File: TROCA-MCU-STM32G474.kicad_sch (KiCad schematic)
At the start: 15 parts, among them SW1 HX-3X6X2.5-X SMD TACT SWITCH, SW2 HX-3X6X2.5-X SMD TACT SWITCH, U3 STM32G474VETx, X1 X32258MOB4SI

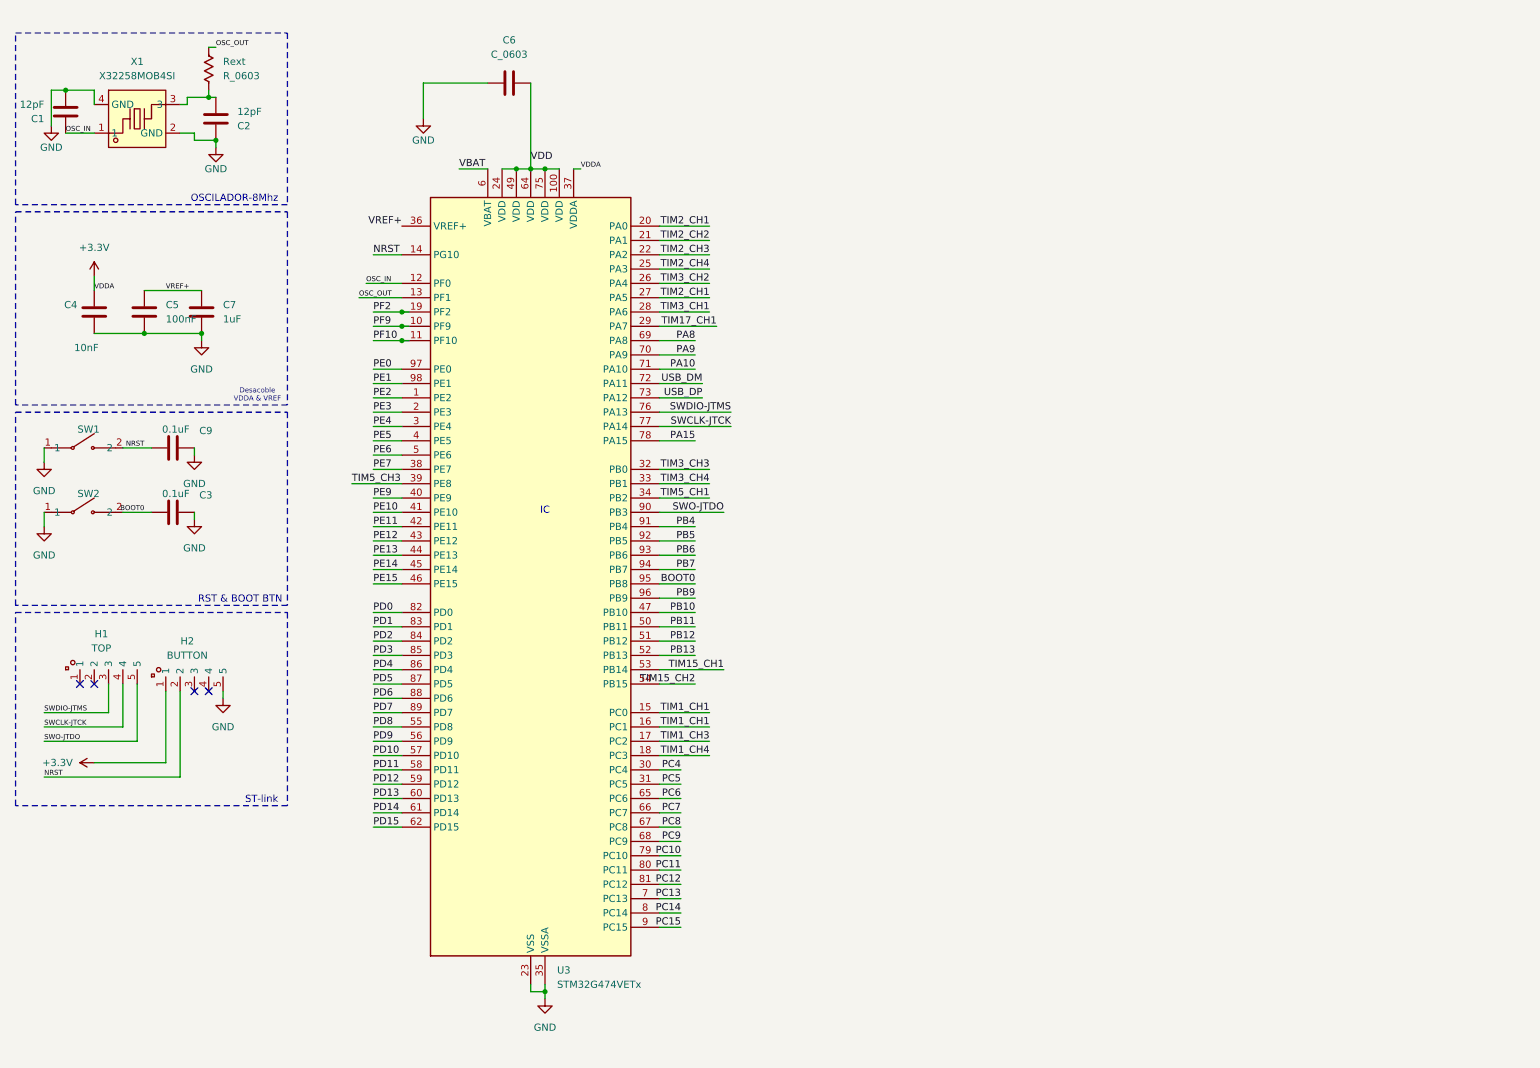
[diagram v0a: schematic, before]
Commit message: Datasheet stm32G474 añadido & declaracion de pines
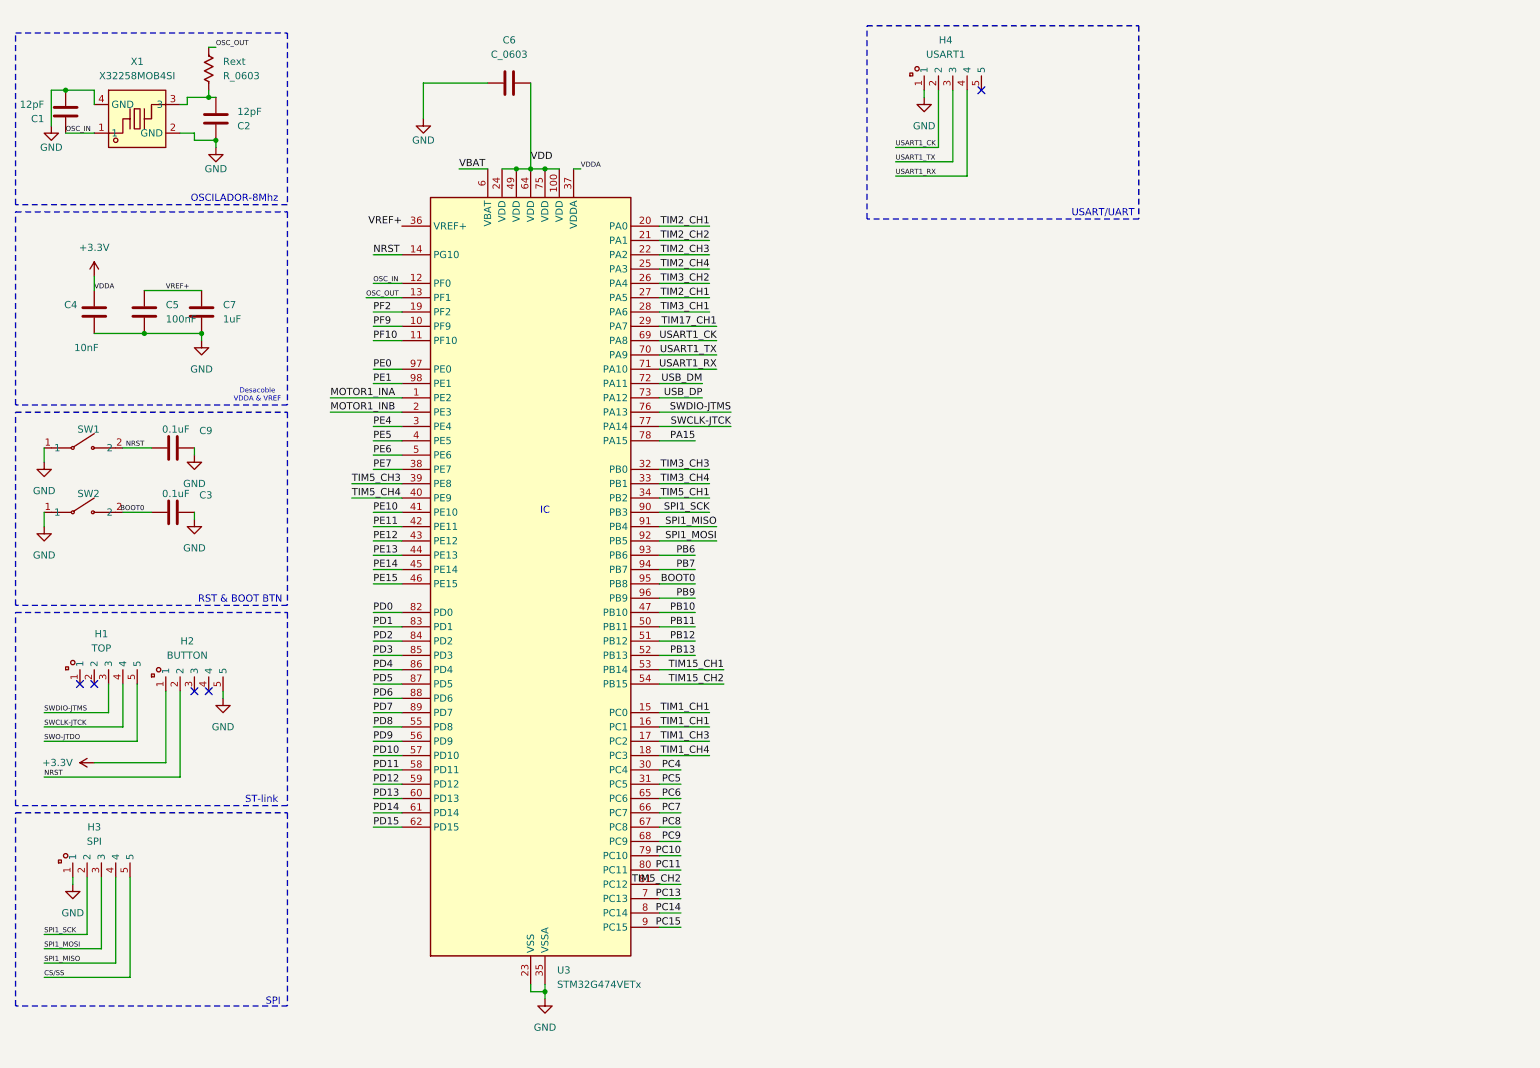
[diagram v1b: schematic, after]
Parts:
- added H3: SPI, EasyEDA:HDR-TH_5P-P2.00-V-M, symbol EasyEDA:HXPZ2.0-1X5PZZ
- added H4: USART1, EasyEDA:HDR-TH_5P-P2.00-V-M, symbol EasyEDA:HXPZ2.0-1X5PZZ
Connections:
- net GND: now also H3.1, H4.1
- net SWO-JTDO: no longer U3.90 (PB3)
- net PA10 renamed USART1_RX
- net USART1_RX: now also H4.4
- net PA8 renamed USART1_CK
- net USART1_CK: now also H4.2
- net PA9 renamed USART1_TX
- net USART1_TX: now also H4.3
- net PB4 renamed SPI1_MISO
- net SPI1_MISO: now also H3.4
- net PB5 renamed SPI1_MOSI
- net SPI1_MOSI: now also H3.3
- net PC12 renamed TIM5_CH2
- net PE2 renamed MOTOR1_INA
- net PE3 renamed MOTOR1_INB
- net PE9 renamed TIM5_CH4
- new net CS/SS: H3.5
- new net SPI1_SCK: H3.2, U3.90 (PB3)
- no-connect marks 4 -> 5
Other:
- note added: "SPI"
- note added: "USART/UART"

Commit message: Delcaracion de INA & INB drivers de motores
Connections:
- net PD0 renamed MOTOR6_INA
- net PD1 renamed MOTOR6_INB
- net PD2 renamed MOTOR7_INA
- net PD3 renamed MOTOR7_INB
- net PD4 renamed MOTOR8_INA
- net PD5 renamed MOTOR8_INB
- net PE10 renamed MOTOR4_INA
- net PE11 renamed MOTOR4_INB
- net PE12 renamed MOTOR5_INA
- net PE13 renamed MOTOR5_INB
- net PE4 renamed MOTOR2_INA
- net PE5 renamed MOTOR2_INB
- net PE6 renamed MOTOR3_INA
- net PE7 renamed MOTOR3_INB
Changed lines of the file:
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@@
 	(wire
 		(pts
-			(xy 80.01 104.14) (xy 85.09 104.14)
+			(xy 72.39 104.14) (xy 85.09 104.14)
 		)
 		(stroke
@@
 	(wire
 		(pts
-			(xy 80.01 121.92) (xy 85.09 121.92)
+			(xy 72.39 121.92) (xy 85.09 121.92)
 		)
 		(stroke
@@
 	(wire
 		(pts
-			(xy 80.01 86.36) (xy 85.09 86.36)
+			(xy 72.39 86.36) (xy 85.09 86.36)
 		)
 		(stroke
@@
 	(wire
 		(pts
-			(xy 80.01 88.9) (xy 85.09 88.9)
+			(xy 72.39 88.9) (xy 85.09 88.9)
 		)
 		(stroke
@@
 	(wire
 		(pts
-			(xy 80.01 127) (xy 85.09 127)
+			(xy 72.39 127) (xy 85.09 127)
 		)
 		(stroke
@@
 	(wire
 		(pts
-			(xy 134.62 167.64) (xy 130.81 167.64)
+			(xy 139.7 167.64) (xy 130.81 167.64)
 		)
 		(stroke
@@
 	(wire
 		(pts
-			(xy 80.01 101.6) (xy 85.09 101.6)
+			(xy 72.39 101.6) (xy 85.09 101.6)
 		)
 		(stroke
@@
 	(wire
 		(pts
-			(xy 80.01 132.08) (xy 85.09 132.08)
-		)
-		(stroke
-			(width 0)
-			(type default)
-		)
-	)
-	(wire
-		(pts
-			(xy 80.01 129.54) (xy 85.09 129.54)
+			(xy 72.39 132.08) (xy 85.09 132.08)
+		)
+		(stroke
+			(width 0)
+			(type default)
+		)
+	)
+	(wire
+		(pts
+			(xy 72.39 129.54) (xy 85.09 129.54)
 		)
 		(stroke
@@
 	(wire
 		(pts
-			(xy 80.01 119.38) (xy 85.09 119.38)
+			(xy 72.39 119.38) (xy 85.09 119.38)
 		)
 		(stroke
@@
 	(wire
 		(pts
-			(xy 80.01 93.98) (xy 85.09 93.98)
+			(xy 72.39 93.98) (xy 85.09 93.98)
 		)
 		(stroke
@@
 	(wire
 		(pts
-			(xy 80.01 124.46) (xy 85.09 124.46)
+			(xy 72.39 124.46) (xy 85.09 124.46)
 		)
 		(stroke
@@
 	(wire
 		(pts
-			(xy 80.01 91.44) (xy 85.09 91.44)
+			(xy 72.39 91.44) (xy 85.09 91.44)
 		)
 		(stroke
@@
 		)
 	)
-	(label "PE6"
-		(at 80.01 91.44 0)
+	(label "MOTOR3_INA"
+		(at 72.39 91.44 0)
 		(effects
 			(font
@@
 		)
 	)
-	(label "PD5"
-		(at 80.01 132.08 0)
+	(label "MOTOR8_INB"
+		(at 72.39 132.08 0)
 		(effects
 			(font
@@
 		)
 	)
-	(label "PD0"
-		(at 80.01 119.38 0)
+	(label "MOTOR6_INA"
+		(at 72.39 119.38 0)
 		(effects
 			(font
@@
 		)
 	)
-	(label "PE11"
-		(at 80.01 104.14 0)
+	(label "MOTOR4_INB"
+		(at 72.39 104.14 0)
 		(effects
 			(font
@@
 		)
 	)
-	(label "PE4"
-		(at 80.01 86.36 0)
+	(label "MOTOR2_INA"
+		(at 72.39 86.36 0)
 		(effects
 			(font
@@
 		)
 	)
-	(label "PD4"
-		(at 80.01 129.54 0)
+	(label "MOTOR8_INA"
+		(at 72.39 129.54 0)
 		(effects
 			(font
@@
 		)
 	)
-	(label "PE7"
-		(at 80.01 93.98 0)
+	(label "MOTOR3_INB"
+		(at 72.39 93.98 0)
 		(effects
 			(font
@@
 	)
 	(label "TIM5_CH2"
-		(at 134.62 167.64 180)
+		(at 139.7 167.64 180)
 		(effects
 			(font
@@
 		)
 	)
-	(label "PE10"
-		(at 80.01 101.6 0)
+	(label "MOTOR4_INA"
+		(at 72.39 101.6 0)
 		(effects
 			(font
@@
 		)
 	)
-	(label "PE12"
+	(label "MOTOR5_INA"
 		(at 80.01 106.68 0)
 		(effects
@@
 		)
 	)
-	(label "PD1"
-		(at 80.01 121.92 0)
+	(label "MOTOR6_INB"
+		(at 72.39 121.92 0)
 		(effects
 			(font
@@
 		)
 	)
-	(label "PD3"
-		(at 80.01 127 0)
-		(effects
-			(font
-				(size 1.27 1.27)
-			)
-			(justify left bottom)
-		)
-	)
-	(label "PE5"
-		(at 80.01 88.9 0)
+	(label "MOTOR7_INB"
+		(at 72.39 127 0)
+		(effects
+			(font
+				(size 1.27 1.27)
+			)
+			(justify left bottom)
+		)
+	)
+	(label "MOTOR2_INB"
+		(at 72.39 88.9 0)
 		(effects
 			(font
@@
 		)
 	)
-	(label "PD2"
-		(at 80.01 124.46 0)
+	(label "MOTOR7_INA"
+		(at 72.39 124.46 0)
 		(effects
 			(font
@@
 		)
 	)
-	(label "PE13"
+	(label "MOTOR5_INB"
 		(at 80.01 109.22 0)
 		(effects

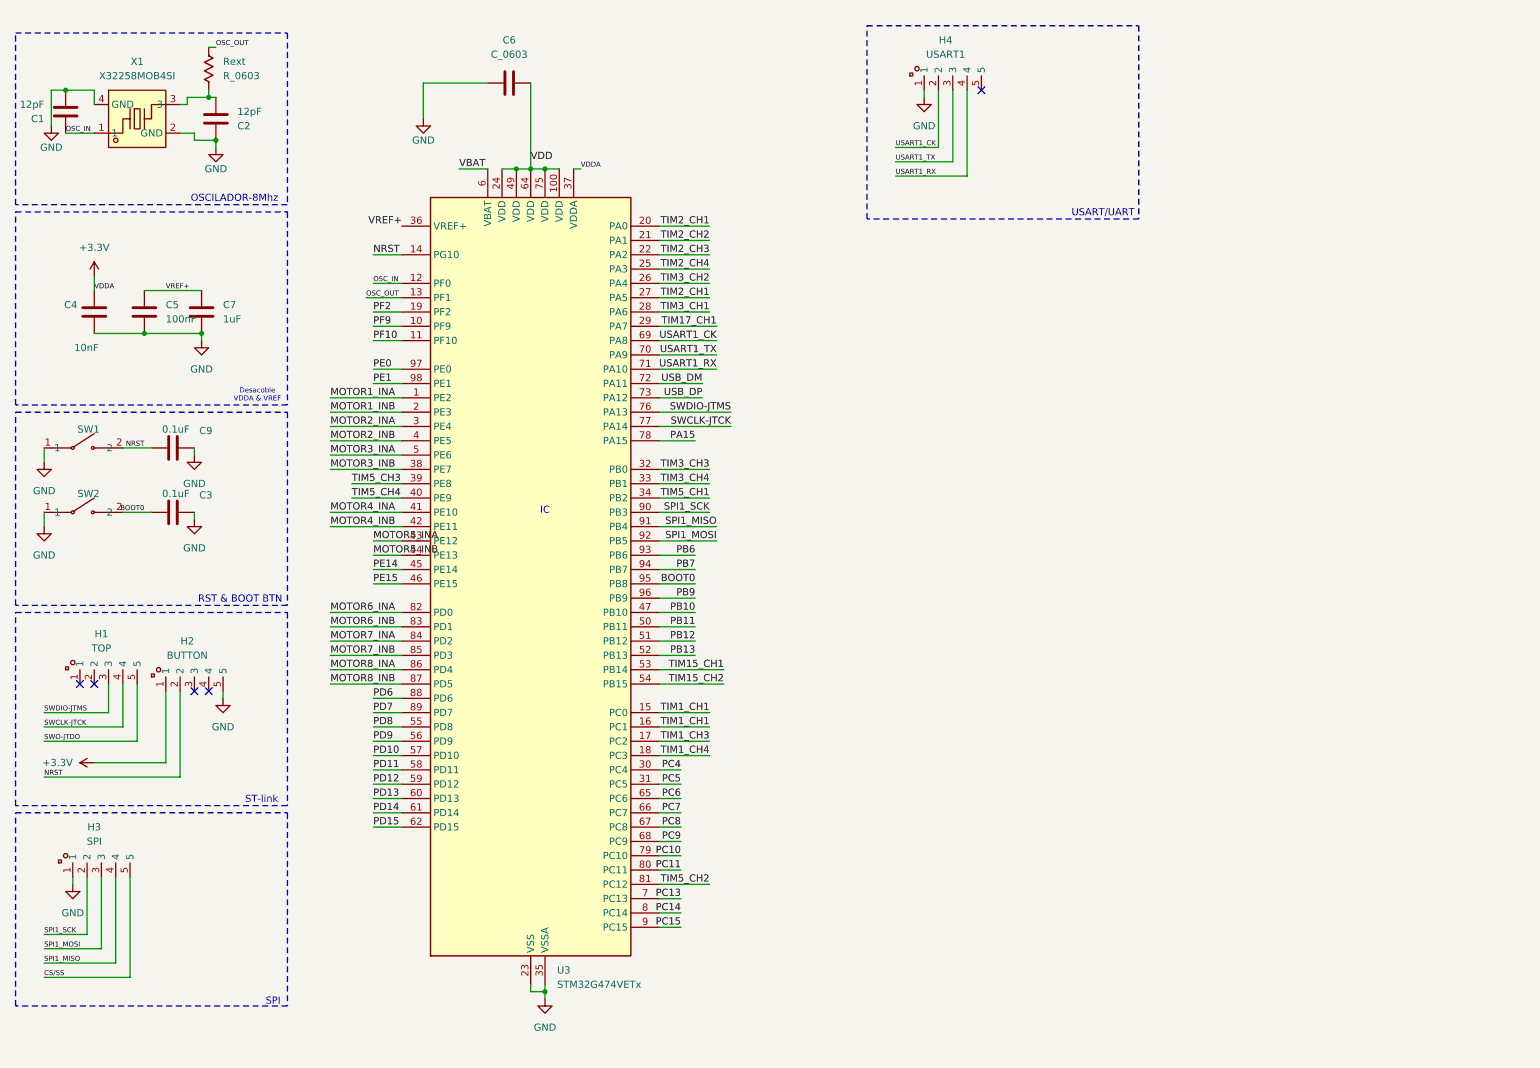
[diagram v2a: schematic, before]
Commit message: Ajustes de asignacion de pines
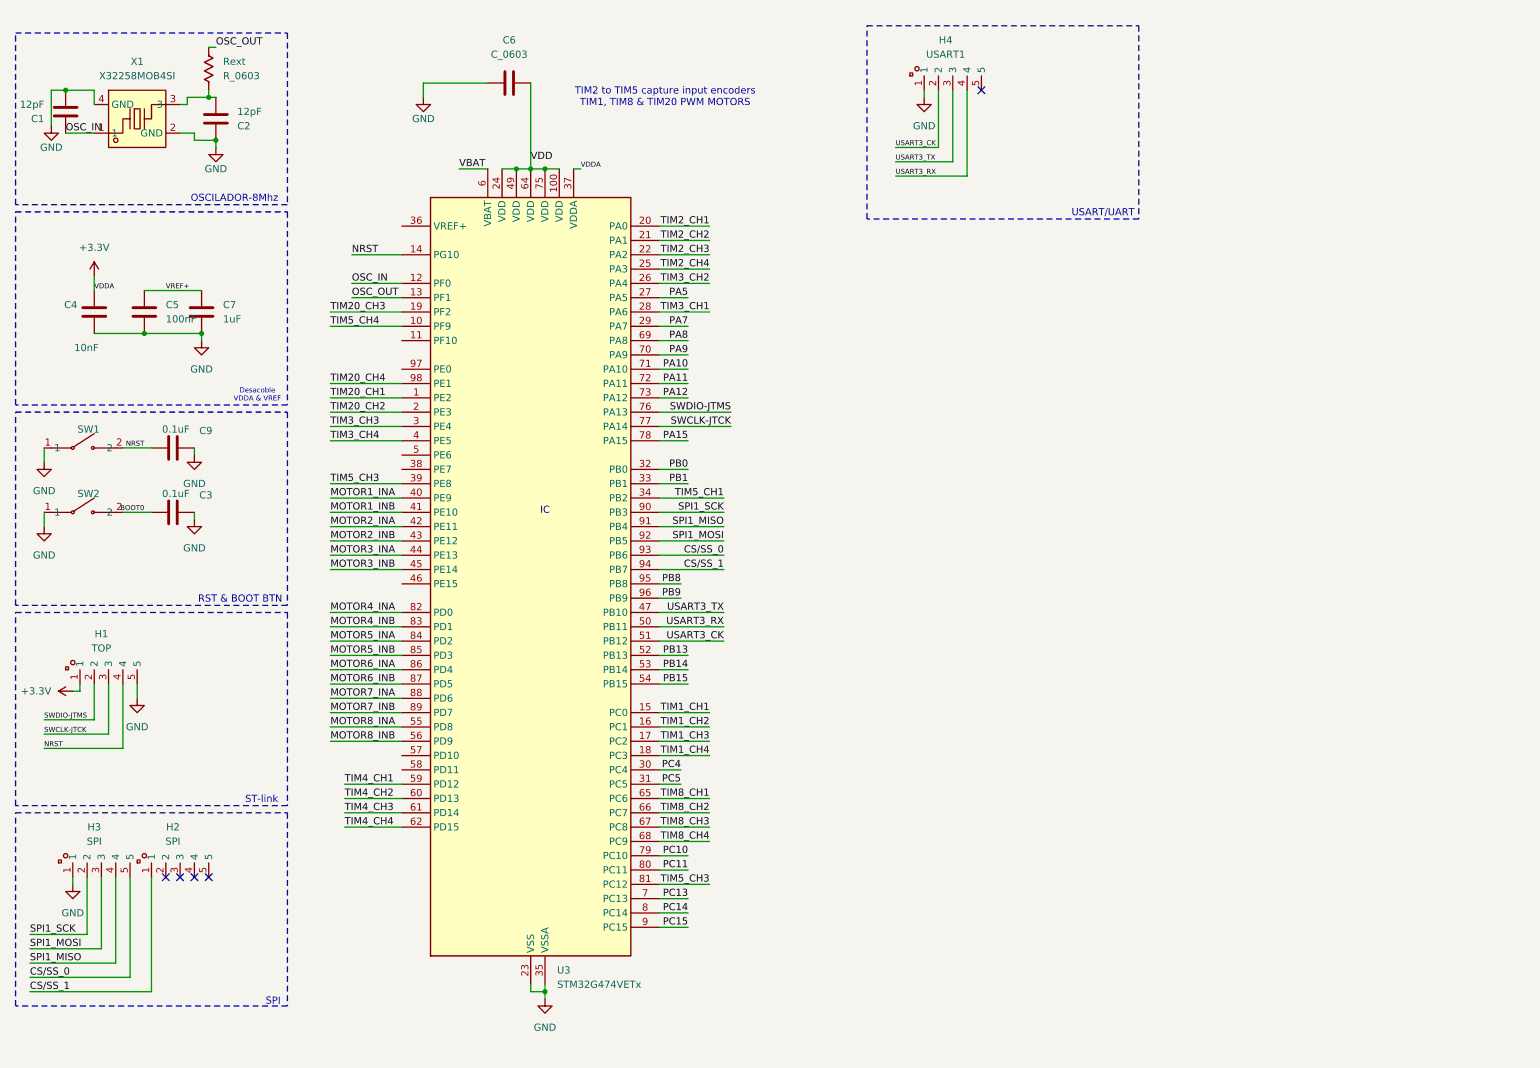
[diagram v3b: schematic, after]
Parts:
- H2: value BUTTON -> SPI
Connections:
- net PB6 is gone; now on net CS/SS_0: U3.93 (PB6)
- net PD6 is gone; now on net MOTOR7_INA: U3.88 (PD6)
- net PD7 is gone; now on net MOTOR7_INB: U3.89 (PD7)
- net PD8 is gone; now on net MOTOR8_INA: U3.55 (PD8)
- net PD9 is gone; now on net MOTOR8_INB: U3.56 (PD9)
- net PE14 is gone; now on net MOTOR3_INB: U3.45 (PE14)
- net PF9 is gone; now on net TIM5_CH4: U3.10 (PF9)
- net SWO-JTDO is gone; now on net GND: H1.5
- net TIM5_CH2 is gone; now on net TIM5_CH3: U3.81 (PC12)
- net +3.3V: now also H1.1; no longer H2.1
- net BOOT0: no longer U3.95 (PB8)
- net GND: no longer H2.5
- net MOTOR1_INA: now also U3.40 (PE9); no longer U3.1 (PE2)
- net MOTOR1_INB: now also U3.41 (PE10); no longer U3.2 (PE3)
- net MOTOR2_INA: now also U3.42 (PE11); no longer U3.3 (PE4)
- net MOTOR2_INB: now also U3.43 (PE12); no longer U3.4 (PE5)
- net MOTOR3_INA: now also U3.44 (PE13); no longer U3.5 (PE6)
- net MOTOR3_INB: no longer U3.38 (PE7)
- net MOTOR4_INA: now also U3.82 (PD0); no longer U3.41 (PE10)
- net MOTOR4_INB: now also U3.83 (PD1); no longer U3.42 (PE11)
- net MOTOR5_INA: now also U3.84 (PD2); no longer U3.43 (PE12)
- net MOTOR5_INB: now also U3.85 (PD3); no longer U3.44 (PE13)
- net MOTOR6_INA: now also U3.86 (PD4); no longer U3.82 (PD0)
- net MOTOR6_INB: now also U3.87 (PD5); no longer U3.83 (PD1)
- net MOTOR7_INA: no longer U3.84 (PD2)
- net MOTOR7_INB: no longer U3.85 (PD3)
- net MOTOR8_INA: no longer U3.86 (PD4)
- net MOTOR8_INB: no longer U3.87 (PD5)
- net NRST: now also H1.4; no longer H2.2
- net SWCLK-JTCK: now also H1.3; no longer H1.4
- net SWDIO-JTMS: now also H1.2; no longer H1.3
- net TIM1_CH1: no longer U3.16 (PC1)
- net TIM2_CH1: no longer U3.27 (PA5)
- net TIM3_CH3: now also U3.3 (PE4); no longer U3.32 (PB0)
- net TIM3_CH4: now also U3.4 (PE5); no longer U3.33 (PB1)
- net TIM5_CH4: no longer U3.40 (PE9)
- net VREF+: no longer U3.36 (VREF+)
- net CS/SS renamed CS/SS_0
- net PB10 renamed USART3_TX
- net USART3_TX: now also H4.3
- net PB11 renamed USART3_RX
- net USART3_RX: now also H4.4
- net PB12 renamed USART3_CK
- net USART3_CK: now also H4.2
- net PB7 renamed CS/SS_1
- net CS/SS_1: now also H2.1
- net PC6 renamed TIM8_CH1
- net PC7 renamed TIM8_CH2
- net PC8 renamed TIM8_CH3
- net PC9 renamed TIM8_CH4
- net PD10: no longer names the net of U3.57 (PD10)
- net PD11: no longer names the net of U3.58 (PD11)
- net PD12 renamed TIM4_CH1
- net PD13 renamed TIM4_CH2
- net PD14 renamed TIM4_CH3
- net PD15 renamed TIM4_CH4
- net PE0: no longer names the net of U3.97 (PE0)
- net PE1 renamed TIM20_CH4
- net PE15: no longer names the net of U3.46 (PE15)
- net PF10: no longer names the net of U3.11 (PF10)
- net PF2 renamed TIM20_CH3
- net TIM15_CH1 renamed PB14
- net TIM15_CH2 renamed PB15
- net TIM17_CH1 renamed PA7
- net USART1_CK renamed PA8
- net PA8: no longer H4.2
- net USART1_RX renamed PA10
- net PA10: no longer H4.4
- net USART1_TX renamed PA9
- net PA9: no longer H4.3
- net USB_DM renamed PA11
- net USB_DP renamed PA12
- new net PA5: U3.27 (PA5)
- new net PB0: U3.32 (PB0)
- new net PB1: U3.33 (PB1)
- new net PB8: U3.95 (PB8)
- new net TIM1_CH2: U3.16 (PC1)
- new net TIM20_CH1: U3.1 (PE2)
- new net TIM20_CH2: U3.2 (PE3)
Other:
- note added: "TIM2 to TIM5 capture input encoders TIM1, TIM8 & TIM20 PWM MOTORS"

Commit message: Integracion de modulos RF
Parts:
- added U1: ~, symbol Rf_433:rf_433MHz RECEIVER
- added U2: ~, symbol Rf_433:rf_433MHz_transmisor
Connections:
- net +3.3V: now also U1.3 (VDD), U2.4 (VCC)
- net GND: now also U1.6 (GND), U2.3 (GND)
- net RF_DIN_0: now reaches U3.57 (PD10)
- net RF_DIN_0: now also U1.5 (DO)
- net RF_DIN_1: now reaches U3.58 (PD11)
- net RF_DIN_1: now also U1.4 (DO)
- net PC4 renamed RF_DOUT_0
- net RF_DOUT_0: now also U2.1 (DAT)
- net PC5 renamed RF_EN
- net RF_EN: now also U2.2 (EN)
- net TIM2_CH1 renamed MOTOR1_ENCA
- net TIM2_CH2 renamed MOTOR1_ENCB
- net TIM2_CH3 renamed MOTOR2_ENCA
- net TIM2_CH4 renamed MOTOR2_ENCB
- net TIM3_CH1 renamed MOTOR3_ENCA
- net TIM3_CH2 renamed MOTOR3_ENCB
- net TIM3_CH3 renamed MOTOR4_ENCA
- net TIM3_CH4 renamed MOTOR4_ENCB
- net TIM4_CH1 renamed MOTOR5_ENCA
- net TIM4_CH2 renamed MOTOR5_ENCB
- net TIM4_CH3 renamed MOTOR6_ENCA
- net TIM4_CH4 renamed MOTOR6_ENCB
- net TIM5_CH1 renamed MOTOR7_ENCA
- net TIM5_CH3 renamed MOTOR7_ENCB
- net MOTOR7_ENCB: no longer U3.39 (PE8)
- net TIM5_CH4 renamed MOTOR8_ENCB
- new net MOTOR8_ENCA: U3.39 (PE8)
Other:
- note added: "RF_RECIVER/TRANSIVER"
